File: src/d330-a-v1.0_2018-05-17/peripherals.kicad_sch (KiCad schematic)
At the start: 23 parts, among them J1 Conn_01x03, J10 Conn_01x04, J11 Conn_01x04, J13 Conn_01x04, J14 Conn_01x10, J15 Conn_01x08, J16 Conn_01x02, J17 Conn_01x03, J18 Conn_01x03, J2 Conn_01x03, J20 Conn_01x04, J21 Conn_01x04, J3 Conn_01x06, J4 Conn_01x06, J5 Conn_01x04, J6 Conn_01x02, J8 Conn_01x04, J9 Conn_01x04, M1 Conn_01x06, M2 Conn_01x06, M3 Conn_01x02, M4 Conn_01x02, M6 Conn_01x02

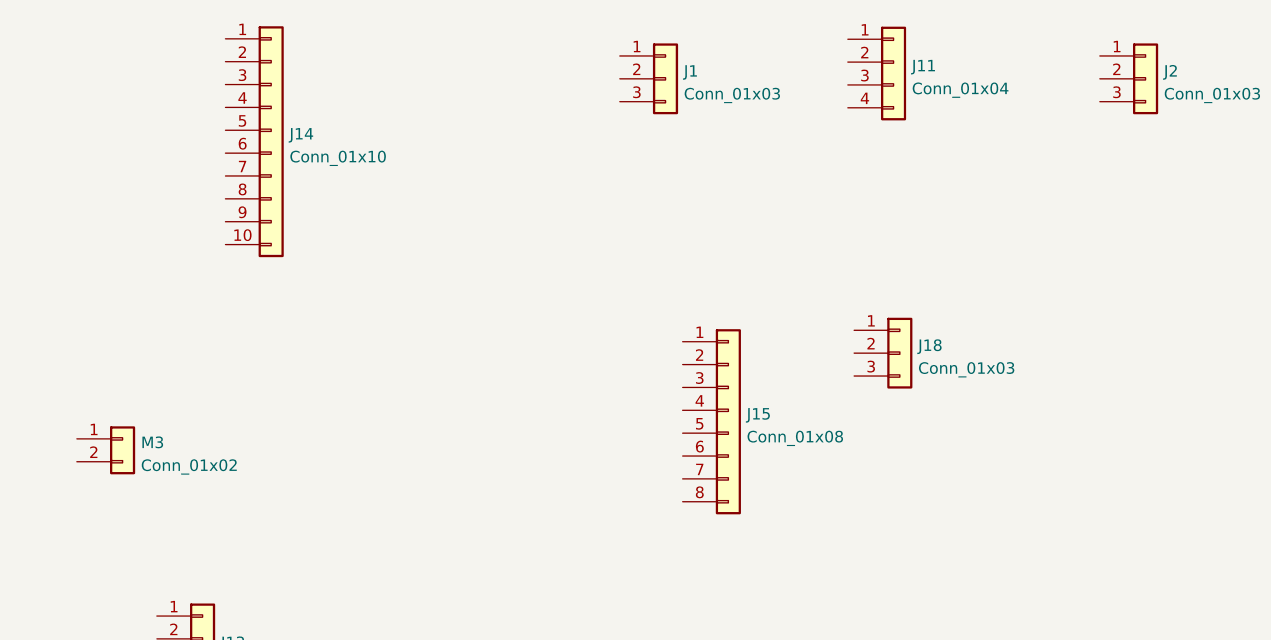
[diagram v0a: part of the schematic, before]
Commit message: Updating connector descriptions
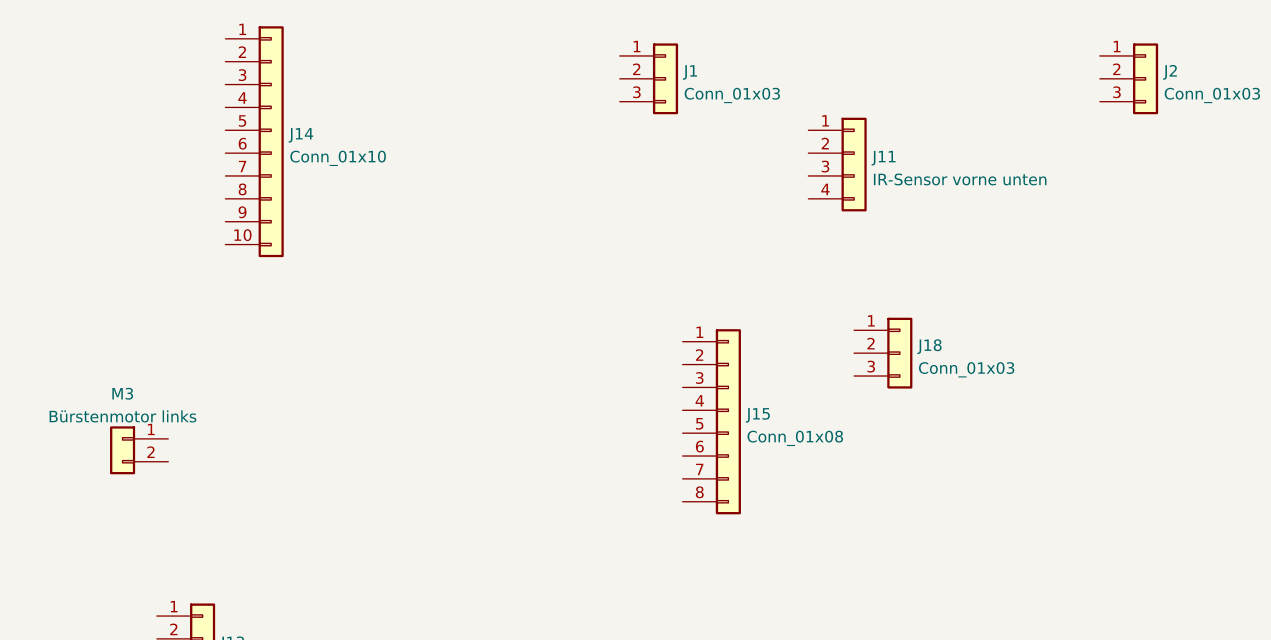
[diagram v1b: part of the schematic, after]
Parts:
- J11: value Conn_01x04 -> IR-Sensor vorne unten
- M3: value Conn_01x02 -> Bürstenmotor links
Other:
- moved on the sheet: J11, M3
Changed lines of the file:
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@@
     (pin "6")
   )
-  (symbol (lib_id "Connector_Generic:Conn_01x04") (at 125.0332 32.4293 0) (unit 1)
-    (in_bom yes) (on_board yes) (fields_autoplaced)
-    (property "Reference" "J11" (id 0) (at 127.0652 32.8646 0)
-      (effects (font (size 1.27 1.27)) (justify left))
-    )
-    (property "Value" "Conn_01x04" (id 1) (at 127.0652 35.4015 0)
-      (effects (font (size 1.27 1.27)) (justify left))
-    )
-    (property "Footprint" "" (id 2) (at 125.0332 32.4293 0)
-      (effects (font (size 1.27 1.27)) hide)
-    )
-    (property "Datasheet" "~" (id 3) (at 125.0332 32.4293 0)
-      (effects (font (size 1.27 1.27)) hide)
-    )
-    (pin "1")
-    (pin "2")
-    (pin "3")
-    (pin "4")
-  )
-  (symbol (lib_id "Connector_Generic:Conn_01x02") (at 39.37 74.295 0) (unit 1)
-    (in_bom yes) (on_board yes) (fields_autoplaced)
-    (property "Reference" "M3" (id 0) (at 41.402 74.7303 0)
-      (effects (font (size 1.27 1.27)) (justify left))
-    )
-    (property "Value" "Conn_01x02" (id 1) (at 41.402 77.2672 0)
-      (effects (font (size 1.27 1.27)) (justify left))
-    )
+  (symbol (lib_id "Connector_Generic:Conn_01x04") (at 120.65 42.545 0) (unit 1)
+    (in_bom yes) (on_board yes) (fields_autoplaced)
+    (property "Reference" "J11" (id 0) (at 122.682 42.9803 0)
+      (effects (font (size 1.27 1.27)) (justify left))
+    )
+    (property "Value" "IR-Sensor vorne unten" (id 1) (at 122.682 45.5172 0)
+      (effects (font (size 1.27 1.27)) (justify left))
+    )
+    (property "Footprint" "" (id 2) (at 120.65 42.545 0)
+      (effects (font (size 1.27 1.27)) hide)
+    )
+    (property "Datasheet" "~" (id 3) (at 120.65 42.545 0)
+      (effects (font (size 1.27 1.27)) hide)
+    )
+    (pin "1")
+    (pin "2")
+    (pin "3")
+    (pin "4")
+  )
+  (symbol (lib_id "Connector_Generic:Conn_01x02") (at 39.37 74.295 0) (mirror y) (unit 1)
+    (in_bom yes) (on_board yes) (fields_autoplaced)
+    (property "Reference" "M3" (id 0) (at 39.37 69.3252 0))
+    (property "Value" "Bürstenmotor links" (id 1) (at 39.37 71.8621 0))
     (property "Footprint" "" (id 2) (at 39.37 74.295 0)
       (effects (font (size 1.27 1.27)) hide)
@@
     )
     (path "/4d30c090-3fd3-43ba-af02-290cb941bb90"
-      (reference "J11") (unit 1) (value "Conn_01x04") (footprint "")
+      (reference "J11") (unit 1) (value "IR-Sensor vorne unten") (footprint "")
     )
     (path "/9a3cfde0-616f-41ca-8548-596fd44a96ae"
@@
     )
     (path "/51b21327-d926-4748-8962-dc7e14e1dbf3"
-      (reference "M3") (unit 1) (value "Conn_01x02") (footprint "")
+      (reference "M3") (unit 1) (value "Bürstenmotor links") (footprint "")
     )
     (path "/d2342a4c-5596-4c9c-9625-8af1fd4219da"
